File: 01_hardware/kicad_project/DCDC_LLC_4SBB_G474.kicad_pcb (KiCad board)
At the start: 4 copper layers, 160 x 105 mm, 237 parts, among them J1 VIN, J2 VOUT, J3 CAN, J4 CAN, J5 ADDR, J6 PROG, J7 SWD, Q1 NCEP0140AG, Q2 NCEP0160AG, Q3 NCEP0160AG, Q4 NCEP0140AG, Q5 NCEP0160AG, Q6 NCEP0160AG, Q7 BSC160N15NS5, Q8 BSC160N15NS5, SW1 DIP-6, T1 PQ2620, U1 STM32G474RBT6, U10 UCC27211DDAR, U11 UCC27524DR, U12 CA-IS3642LVW, U13 LMR16006XDDCR, U14 AMS1117-5.0, U15 LMV331IDBVR, U16 TL431AIDBZR, U2 UCC27211DDAR, U3 UCC27211DDAR, U4 LMR16006XDDCR, U5 AMS1117-5.0, U7 INA181A1IDBVR, U8 INA181A2IDBVR, U9 CA-IS3062VW, Y1 16MHz

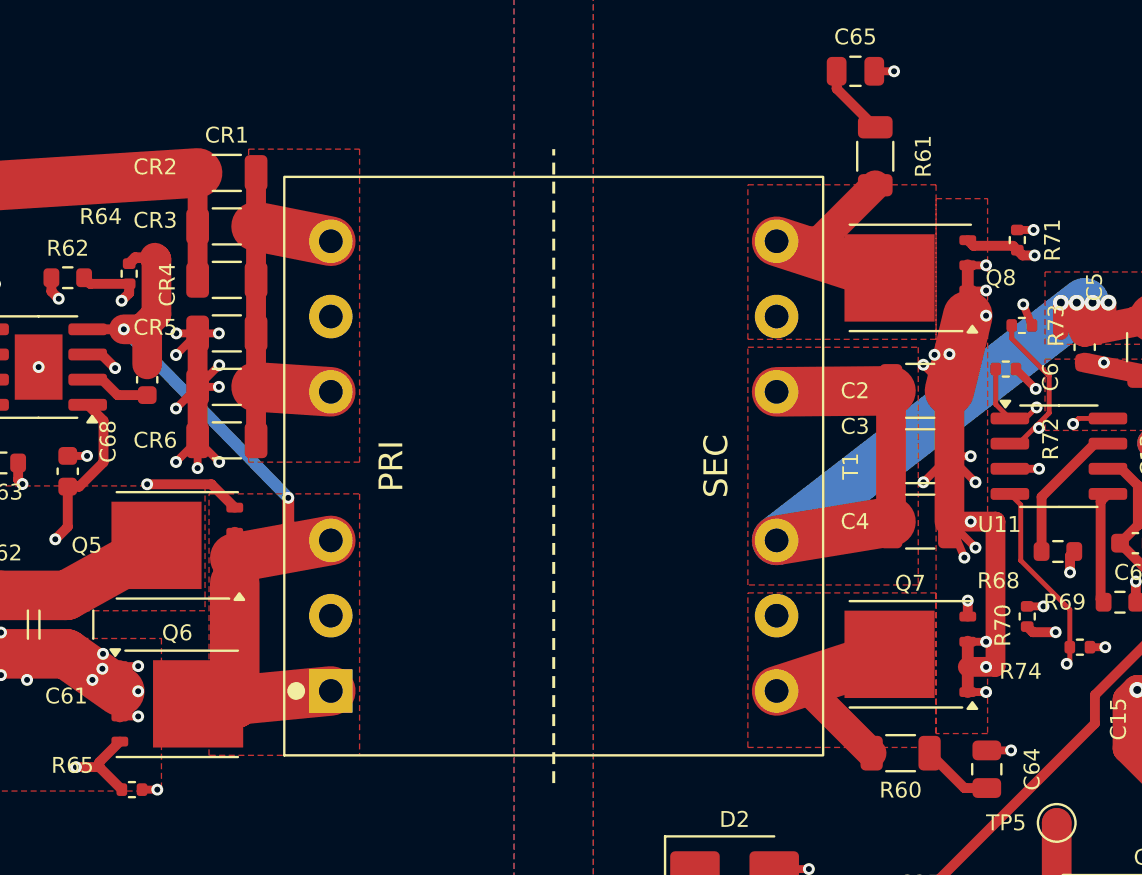
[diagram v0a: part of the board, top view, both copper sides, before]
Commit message: T1: footprint to vendor PQ2620 6+6 bobbin, winding guide update
- TX_PQ2620_12P: 25.4 mm row-to-row (was 22.5 placeholder), 1.1 mm holes
  for 0.70 mm pins, 27 x 29 mm body outline/courtyard
- PCB: track stubs to the new T1 pads; VBUS (In2) and LLC_HI_P/LO_P (In2)
  rerouted clear of the moved pins; CR1-CR6 -0.4 mm, Q7/Q8 +0.1 mm so
  courtyards clear the larger bobbin; C2-C4 refs to F.Fab only
- DRC clean, netlist parity and isolation check pass
- Winding guide: bobbin data, radial fit check (foil primary recommended,
  litz 0.1x200 does not fit), materials updated
- Regenerated gerbers, CPL, EasyEDA import, PCB layer PDF

Co-Authored-By: Claude Opus 5.5 <noreply@anthropic.com>
Claude-Session: https://claude.ai/code/session_01A35wrnwFKLPSaRSxxHs471
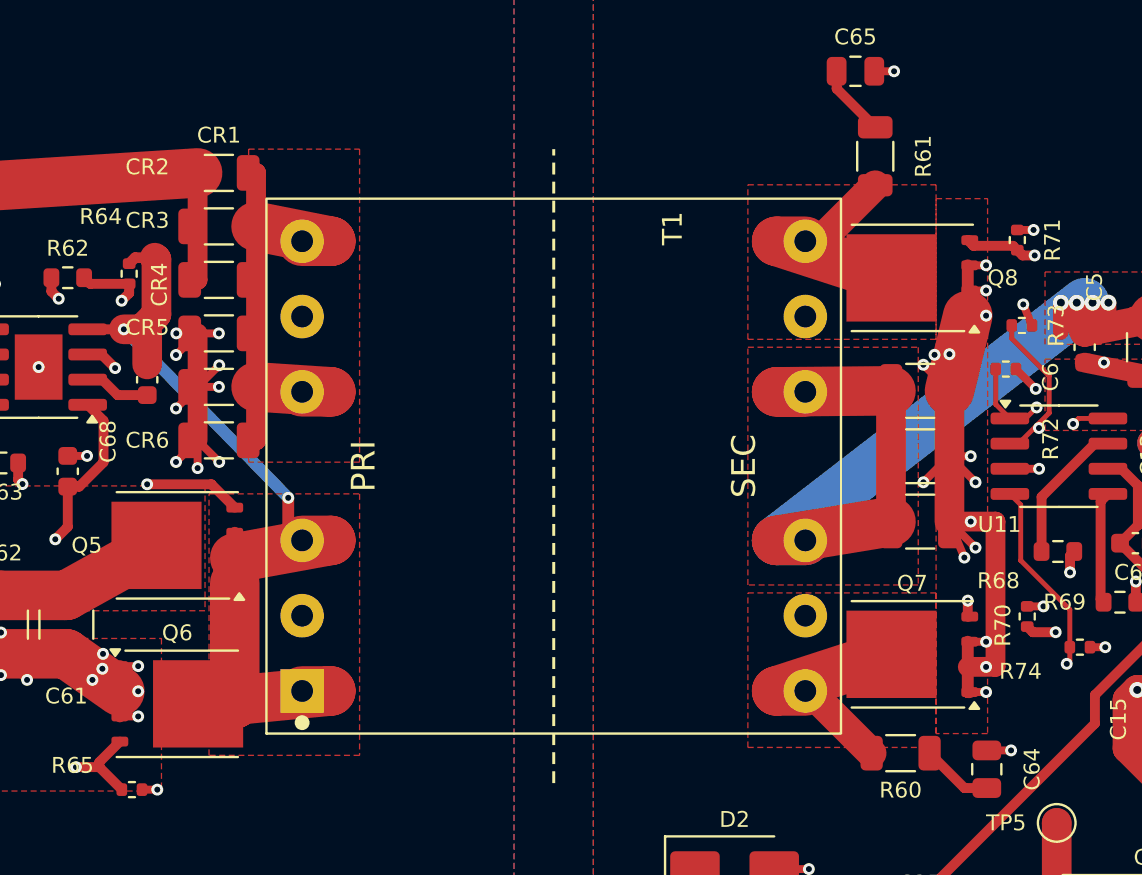
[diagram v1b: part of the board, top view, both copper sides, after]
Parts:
- moved CR1 0.40 mm to (53.1, 15.2)
- moved CR2 0.40 mm to (53.1, 17.9)
- moved CR3 0.40 mm to (53.1, 20.6)
- moved CR4 0.40 mm to (53.1, 23.3)
- moved CR5 0.40 mm to (53.1, 26.0)
- moved CR6 0.40 mm to (53.1, 28.7)
- moved Q7 0.10 mm to (88.1, 39.5)
- moved Q8 0.10 mm to (88.1, 20.5)
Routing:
- net CR_MID: track 24.9 -> 32.3 mm
- net SR_D2: track 15.9 -> 21.8 mm
- net SR_D1: track 15.9 -> 21.8 mm
- net HB_SW: track 50.8 -> 56.6 mm
- net VBUS: track 185.2 -> 188.9 mm
- net GNDP: track 108.8 -> 110.0 mm
- net VIN: track 196.0 -> 196.8 mm
- net GND: track 309.8 -> 310.4 mm

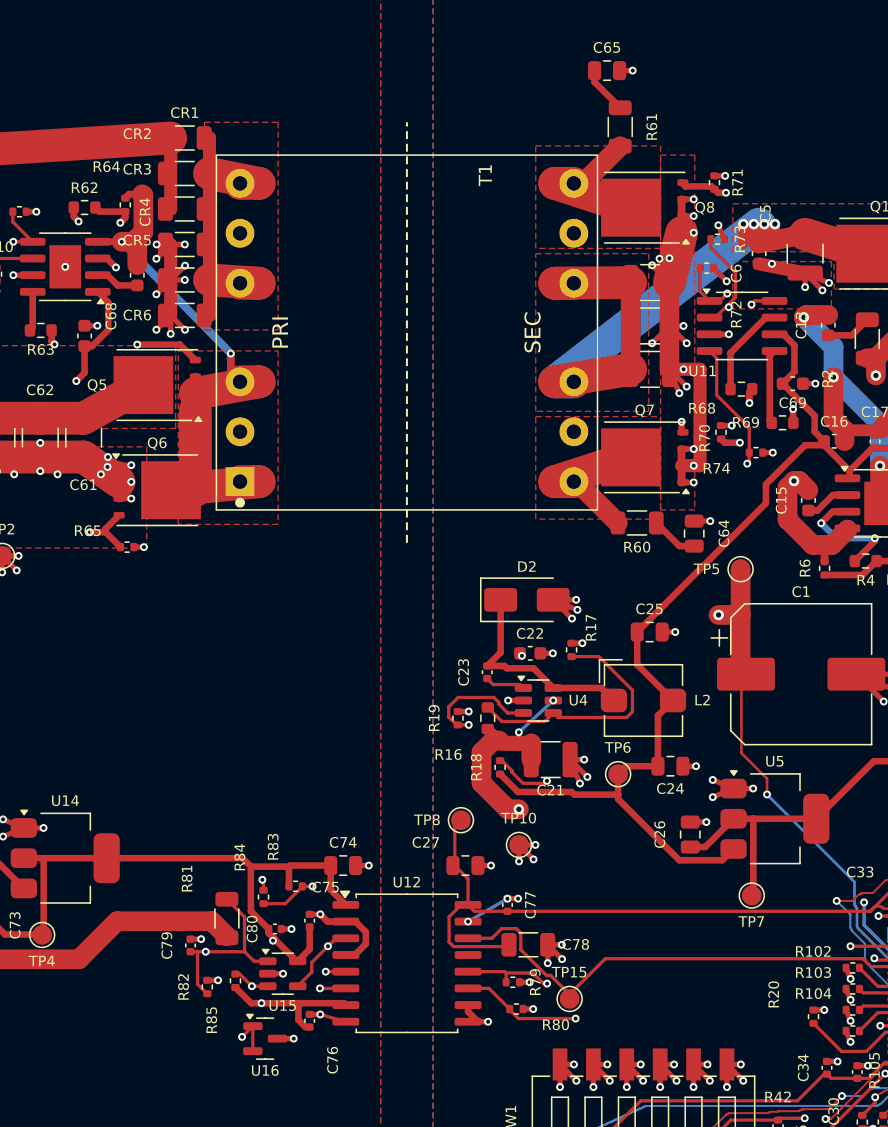
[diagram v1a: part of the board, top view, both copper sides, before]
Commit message: T1: footprint fits PQ2620 and PQ2625 bobbins; SW1 address silkscreen
- TX_PQ2620_12P: 1.2 mm holes (0.70 / 0.80 mm pins, 25.4 / 25.5 mm rows),
  outline and courtyard for the 29.8 x 26.7 mm PQ2625 base
- Room around T1: T1 +0.1 mm, CR1-CR6 -0.7 mm total, Q7/Q8 +0.68 mm total
  with their gate/GND fan-out, R61 +0.3 mm; HB_SW driver return 1.5 -> 0.8 mm,
  GND bus beside Q7 moved to x=92.72, Q8 source strap 2.5 -> 1.6 mm,
  three source-side GND vias stepped out of the pads, three removed
- SW1 silkscreen: A0..A5 per switch and "ON=1"; R80 reference moved
- DRC clean (incl. courtyards), netlist parity and isolation check pass
- Regenerated gerbers, CPL, EasyEDA import, PCB layer PDF

Co-Authored-By: Claude Opus 5.5 <noreply@anthropic.com>
Claude-Session: https://claude.ai/code/session_01A35wrnwFKLPSaRSxxHs471
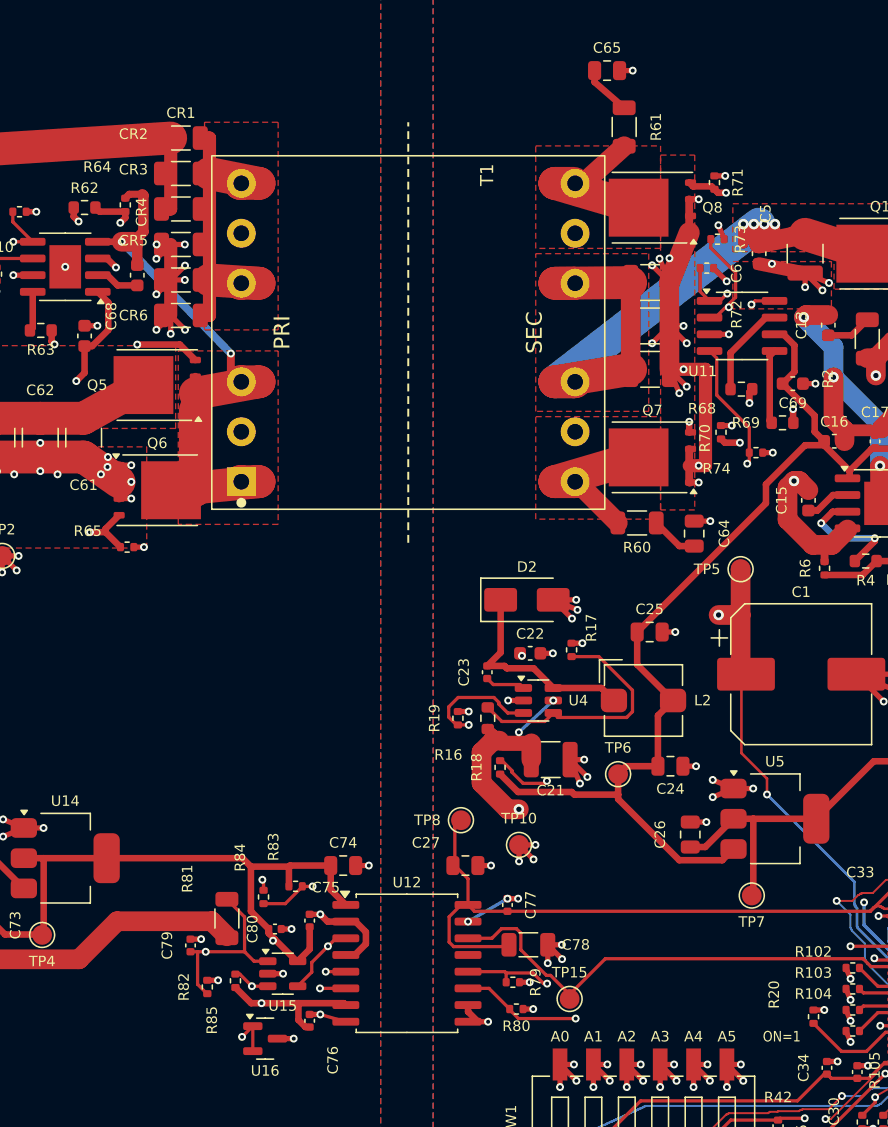
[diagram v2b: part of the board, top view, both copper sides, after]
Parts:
- T1: footprint custom_fp:TX_PQ2620_12P -> TX_PQ2620_12P
- moved Q7 0.58 mm to (88.7, 39.5)
- moved Q8 0.58 mm to (88.7, 20.5)
- moved CR1 0.30 mm to (52.8, 15.2)
- moved CR2 0.30 mm to (52.8, 17.9)
- moved CR3 0.30 mm to (52.8, 20.6)
- moved CR4 0.30 mm to (52.8, 23.3)
- moved CR5 0.30 mm to (52.8, 26.0)
- moved CR6 0.30 mm to (52.8, 28.7)
- moved R61 0.30 mm to (86.5, 14.4)
- moved T1 0.10 mm to (70.1, 30.0)
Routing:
- net GND: track 310.4 -> 307.5 mm, vias 181 -> 178
- net CR_MID: track 32.3 -> 33.8 mm
- net SR_D2: track 21.8 -> 22.8 mm
- net GNDP: track 110.0 -> 110.9 mm
- net SR_D1: track 21.8 -> 22.5 mm
- net VIN: track 196.8 -> 197.4 mm
- net G8: track 24.6 -> 24.0 mm
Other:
- board text added: "A0"
- board text added: "A1"
- board text added: "A2"
- board text added: "A3"
- board text added: "A4"
- board text added: "A5"
- board text added: "ON=1"

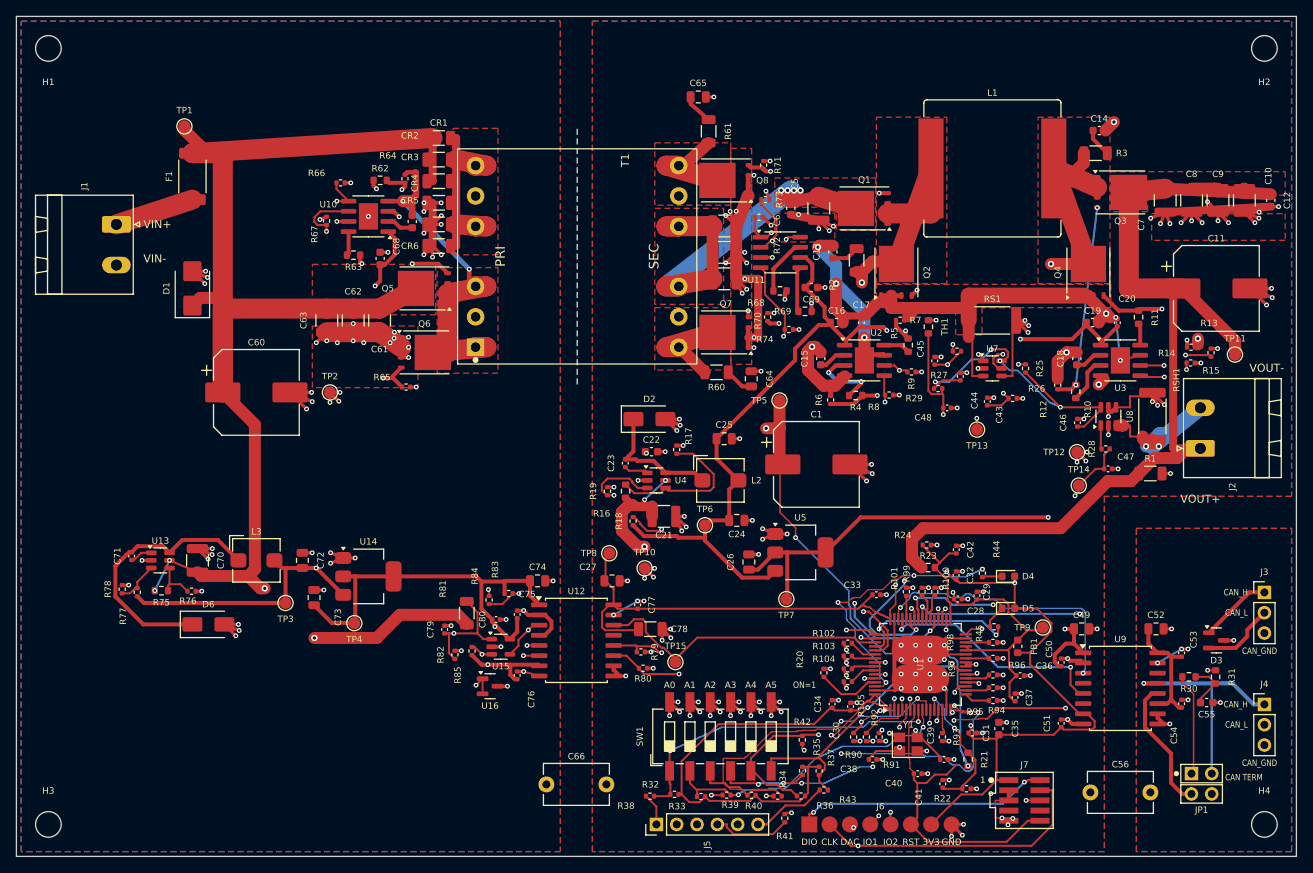
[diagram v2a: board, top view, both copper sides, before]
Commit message: Layout review: power path, switch nodes, gate loops, Kelvin, clean-up
- VOUT pour C11 -> J2 (was one 1.0 mm track; ~10 -> ~3.5 mOhm)
- CR1-CR6: VIN / GNDP pours on the left pads, CR_MID pour over the right pads
- SW1/SW2 pours trimmed to L1 pad + FET pins/tab (282/271 -> 213/211 mm2)
- High-side gate loops: SW1 return beside G1 on In2 (~85 -> ~15 mm2),
  SW2 return beside G3 on B.Cu and G3 0.25 -> 0.5 mm (~47 -> ~18 mm2),
  HB_SW return beside G5 on B.Cu (~17 -> ~8 mm2)
- U8 sense taps moved inside the RSH1 pads (Kelvin)
- Router staircases straightened: 2906 -> 1810 segments, clearance-checked
- 320 ground stitching vias (5 mm grid, only where the ground net is poured
  on all four layers)
- DRC clean, netlist parity, 4.0 mm isolation gaps unchanged
- Scripts in 04_scripts; review picture in 01_hardware/docs

Co-Authored-By: Claude Opus 5.5 <noreply@anthropic.com>
Claude-Session: https://claude.ai/code/session_01A35wrnwFKLPSaRSxxHs471
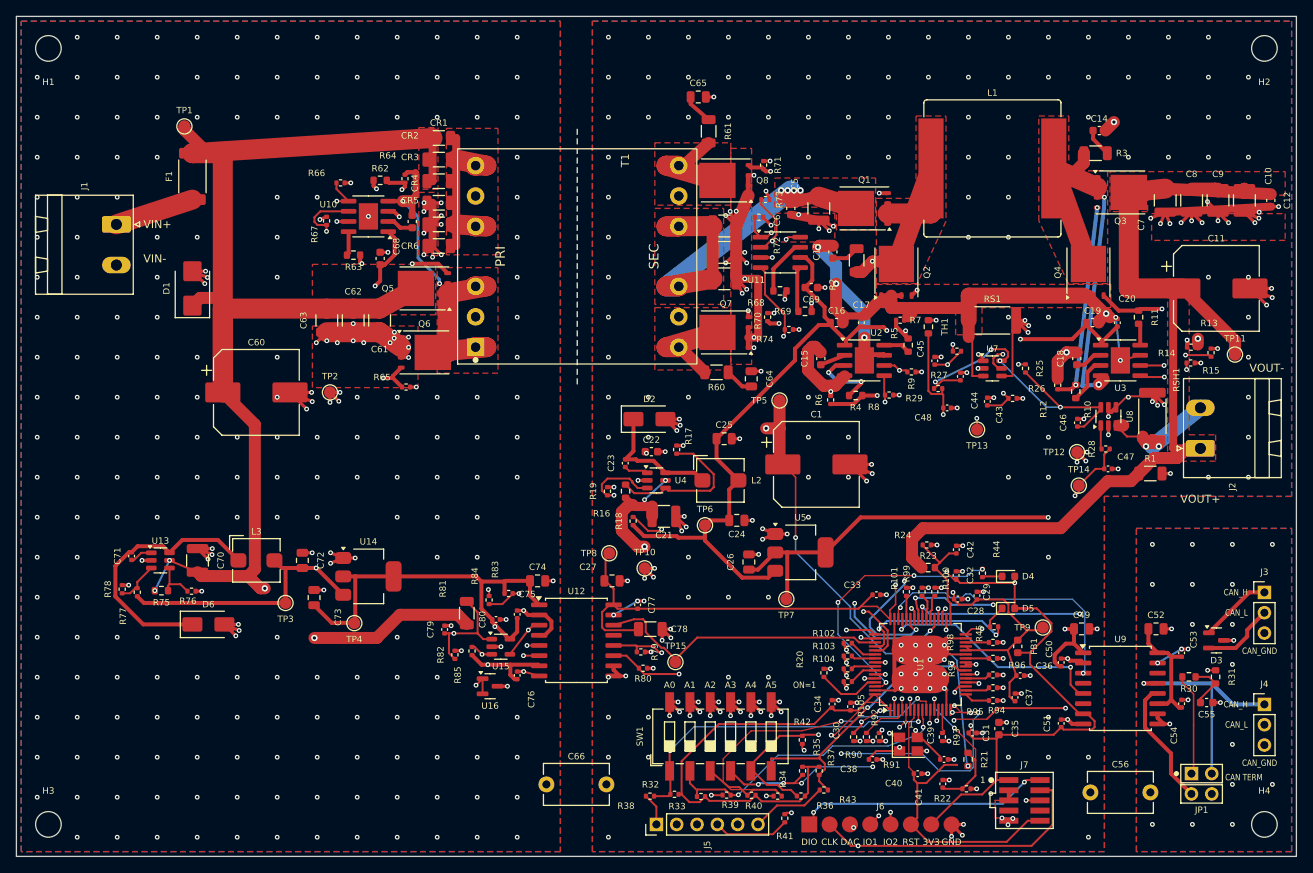
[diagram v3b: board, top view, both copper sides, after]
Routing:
- net SW2: track 54.4 -> 64.6 mm
- net SW1: track 53.8 -> 62.7 mm
- net VOUT_N: track 20.9 -> 17.2 mm
- net SR_EN: track 66.7 -> 63.7 mm
- net SR_D2: track 22.8 -> 19.9 mm
- net SR_D1: track 22.5 -> 19.6 mm
- net CR_MID: track 33.8 -> 30.9 mm
- net TP_DAC: track 30.7 -> 28.3 mm
- net HB_SW: track 56.9 -> 54.8 mm
- net ADDR2: track 51.3 -> 49.9 mm
- net ADDR3: track 38.5 -> 37.4 mm
- net VBUS: track 189.1 -> 188.3 mm
- net +3V3A: track 101.8 -> 101.0 mm
- net CAN_TL: track 17.9 -> 17.2 mm
- net CANL: track 58.6 -> 57.9 mm
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
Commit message: ADDR2 duplicate route removed; contained duplicate segments cleaned
- ADDR2: MCU branch ran parallel to the SW1-R34-R40 track; it now ends
  where it meets that track (single tree)
- 90 same-net segments lying fully inside another track removed
  (no copper change), 5 tiny dangling stubs removed
- DRC clean, netlist parity unchanged

Co-Authored-By: Claude Opus 5.5 <noreply@anthropic.com>
Claude-Session: https://claude.ai/code/session_01A35wrnwFKLPSaRSxxHs471
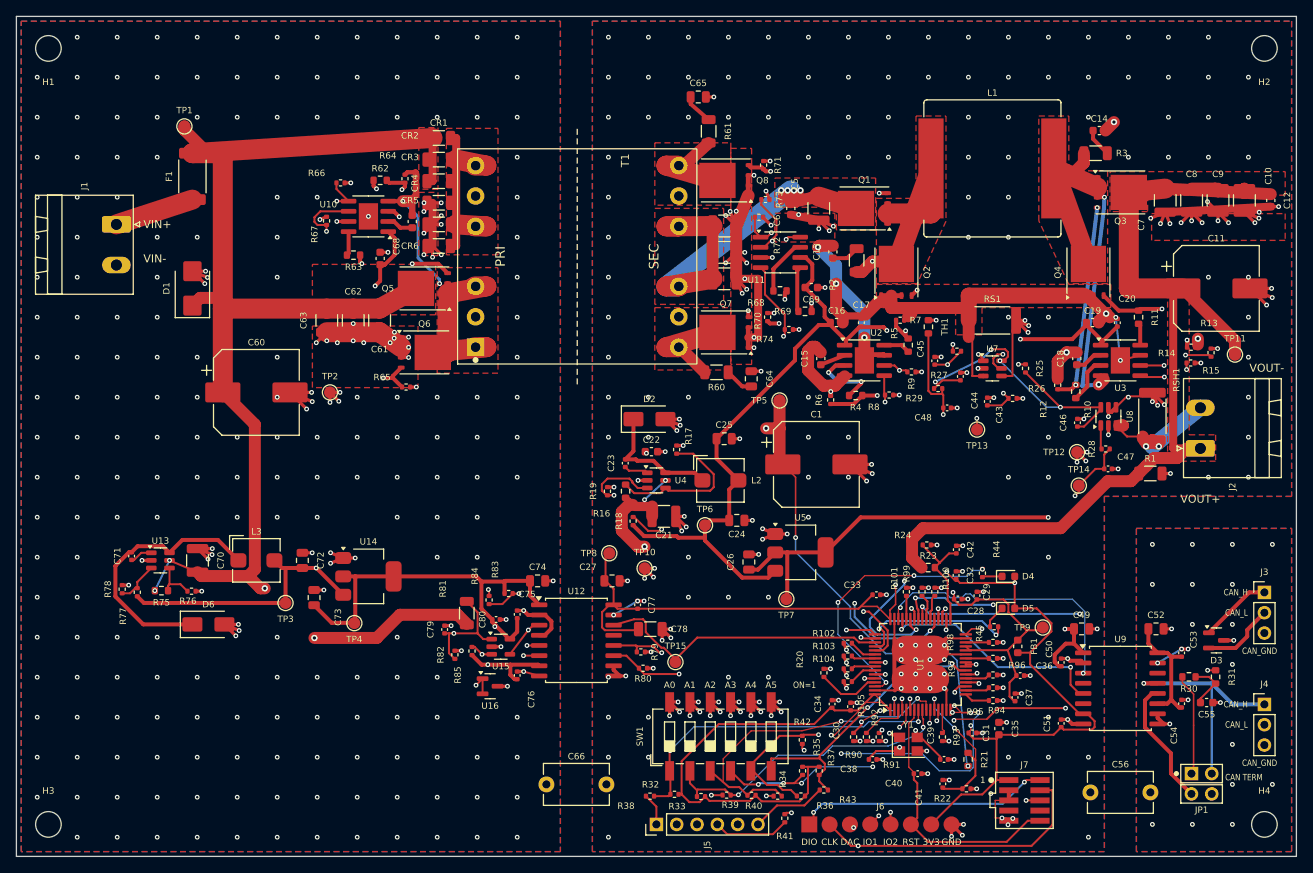
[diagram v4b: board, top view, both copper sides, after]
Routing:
- net VIN: track 197.4 -> 175.0 mm
- net ADDR2: track 49.9 -> 43.0 mm
- net NRST: track 39.5 -> 33.5 mm
- net GND: track 307.6 -> 301.9 mm
- net GNDP: track 110.9 -> 105.4 mm
- net VBUS: track 188.3 -> 185.0 mm
- net +3V3: track 256.4 -> 253.1 mm
- net SR_D1: track 19.6 -> 16.4 mm
- net PGND: track 135.6 -> 132.4 mm
- net VOUT: track 121.1 -> 118.5 mm
- net SR_D2: track 19.9 -> 18.3 mm
- net CR_MID: track 30.9 -> 29.3 mm
- net SW2: track 64.6 -> 63.7 mm
- net +3V3A: track 101.0 -> 100.2 mm
- net ADDR4: track 56.4 -> 55.8 mm
